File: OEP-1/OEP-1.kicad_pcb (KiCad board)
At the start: 2 copper layers, 18 parts

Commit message: готова трассировка, подготовлены файлы производства (45х30)мм)
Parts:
- added C1: Конденсатор_К10-83-25В-0,1_мкФ+-20проц., MOTOR_RLC:Конденсатор_SMD_IEC_0805, F.Cu at (109.2, 155.8)
- added C2: Конденсатор_К53-56А-32В-22_мкФ+-10проц., MOTOR_RLC:Конденсатор_тантал_SMD_m7343, F.Cu at (133.5, 148.2)
- added C3: Конденсатор_К10-83-25В-0,1_мкФ+-20проц., MOTOR_RLC:Конденсатор_SMD_IEC_0805, F.Cu at (117.0, 157.2)
- added C4: Конденсатор_К10-83-25В-0,1_мкФ+-20проц., MOTOR_RLC:Конденсатор_SMD_IEC_0805, F.Cu at (127.2, 159.0)
- added C5: Конденсатор_К10-83-25В-0,1_мкФ+-20проц., MOTOR_RLC:Конденсатор_SMD_IEC_0805, F.Cu at (125.0, 159.0)
- added C6: Конденсатор_К10-83-25В-0,1_мкФ+-20проц., MOTOR_RLC:Конденсатор_SMD_IEC_0805, F.Cu at (137.2, 147.5)
- added R13: Резистор_0,125Вт, MOTOR_RLC:Резистор_SMD_IEC_0805_0,125_Вт, F.Cu at (112.0, 167.2)
- added R14: Резистор_0,125Вт, MOTOR_RLC:Резистор_SMD_IEC_0805_0,125_Вт, F.Cu at (133.0, 152.5)
- added X1: Клеммник_х6, MOTOR_X:Вилка_СНП389-6ВП32-1-1, F.Cu at (105.5, 153.4)
- added X2: Клеммник_х6, MOTOR_X:Вилка_СНП389-6ВП32-1-1, F.Cu at (139.5, 166.2)
- added X3: Контрольная_точка_сопряжения, MOTOR_X:Пробник, B.Cu at (109.8, 156.0)
- added X4: Крепежное_отверстие_М3, MOTOR_ICO:Крепежное_Отверстие_под_М3, F.Cu at (103.0, 172.0)
- added X5: Крепежное_отверстие_М3, MOTOR_ICO:Крепежное_Отверстие_под_М3, F.Cu at (102.8, 147.8)
- added X6: Крепежное_отверстие_М3, MOTOR_ICO:Крепежное_Отверстие_под_М3, F.Cu at (142.0, 172.0)
- added X7: Крепежное_отверстие_М3, MOTOR_ICO:Крепежное_Отверстие_под_М3, F.Cu at (142.0, 148.0)
- R1, R10, R11, R12, R2, R3, R4, R5, R6, R7, R8, R9: footprint N_RLC:Резистор_SMD_0805_0,125Вт -> MOTOR_RLC:Резистор_SMD_IEC_0805_0,125_Вт
- moved R9 194.7 mm to (131.0, 170.8), turned to 180 degrees
- moved R4 193.4 mm to (123.0, 167.8), turned to 270 degrees
- moved DD1 187.8 mm to (111.2, 159.8), turned to 90 degrees
- moved R11 186.9 mm to (126.5, 163.0)
- moved VT1 186.8 mm to (119.2, 167.5), turned to 180 degrees
- moved VT2 183.6 mm to (130.0, 167.5), turned to 180 degrees
- moved R5 182.3 mm to (120.2, 170.8), turned to 180 degrees
- moved R1 180.8 mm to (112.2, 164.0), turned to 180 degrees
- moved R8 178.9 mm to (133.8, 167.8), turned to 270 degrees
- moved R6 176.2 mm to (126.8, 153.8), turned to 180 degrees
- moved R3 175.0 mm to (125.5, 167.8), turned to 270 degrees
- moved R10 174.7 mm to (136.2, 167.8), turned to 270 degrees
- moved DD2 174.6 mm to (133.8, 159.9), turned to 270 degrees
- moved R2 173.3 mm to (115.0, 154.0)
- moved R12 173.0 mm to (132.8, 155.8)
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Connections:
- DD1 pad 6: Net-(DD1-Pad6) -> /CAN-L-1
- DD1 pad 7: Net-(DD1-Pad7) -> /CAN-H-1
- DD2 pad 6: Net-(DD2-Pad6) -> /CAN-L-2
- DD2 pad 7: Net-(DD2-Pad7) -> /CAN-H-2
- G1 pad 1: Net-(G1-Pad1) -> /PWR
- G1 pad 3: Net-(G1-Pad3) -> /5V
- G1 pad 4: Net-(G1-Pad4) -> /GND
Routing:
- net /5V: track 0.00 -> 126.1 mm, vias 0 -> 2
- net /PWR: track 0.00 -> 68.9 mm
- net /TX-1: track 0.00 -> 63.3 mm, vias 0 -> 2
- net /PWR_GND: track 0.00 -> 60.2 mm
- net /GND: track 0.00 -> 45.0 mm, vias 0 -> 9
- net /TX-2: track 0.00 -> 35.2 mm
- net /CAN-L-1: track 0.00 -> 20.0 mm
- net /CAN-L-2: track 0.00 -> 19.9 mm
- net /RX-1: track 0.00 -> 15.9 mm, vias 0 -> 2
- net /RX-2: track 0.00 -> 13.2 mm, vias 0 -> 2
- net Net-(R13-Pad1): track 0.00 -> 10.4 mm
- net Net-(R14-Pad1): track 0.00 -> 10.4 mm
- net Net-(R8-Pad2): track 0.00 -> 7.16 mm
- net Net-(R4-Pad2): track 0.00 -> 7.16 mm
- net Net-(DA1-Pad6): track 0.00 -> 6.96 mm
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- added copper zone on B.Cu, net /GND
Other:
- board outline added: 45 x 30 mm
- net class 5V added: clearance 0.2, trace_width 0.45, via_dia 0.8, via_drill 0.4
- net class PWR added: clearance 0.4, trace_width 1, via_dia 0.8, via_drill 0.4
- board text added: "OEP-1-0N6"

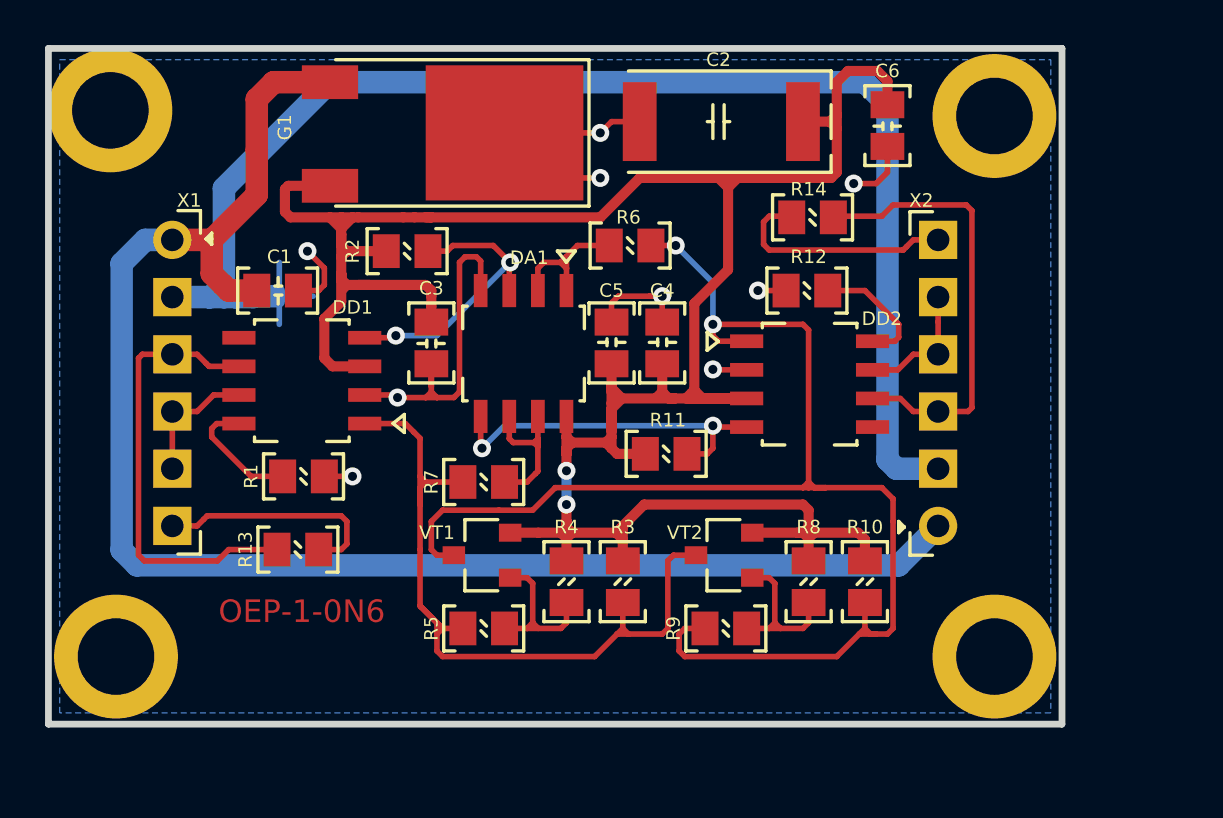
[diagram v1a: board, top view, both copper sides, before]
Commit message: ОУ заменен на транзисторный каскад (50х30 мм)
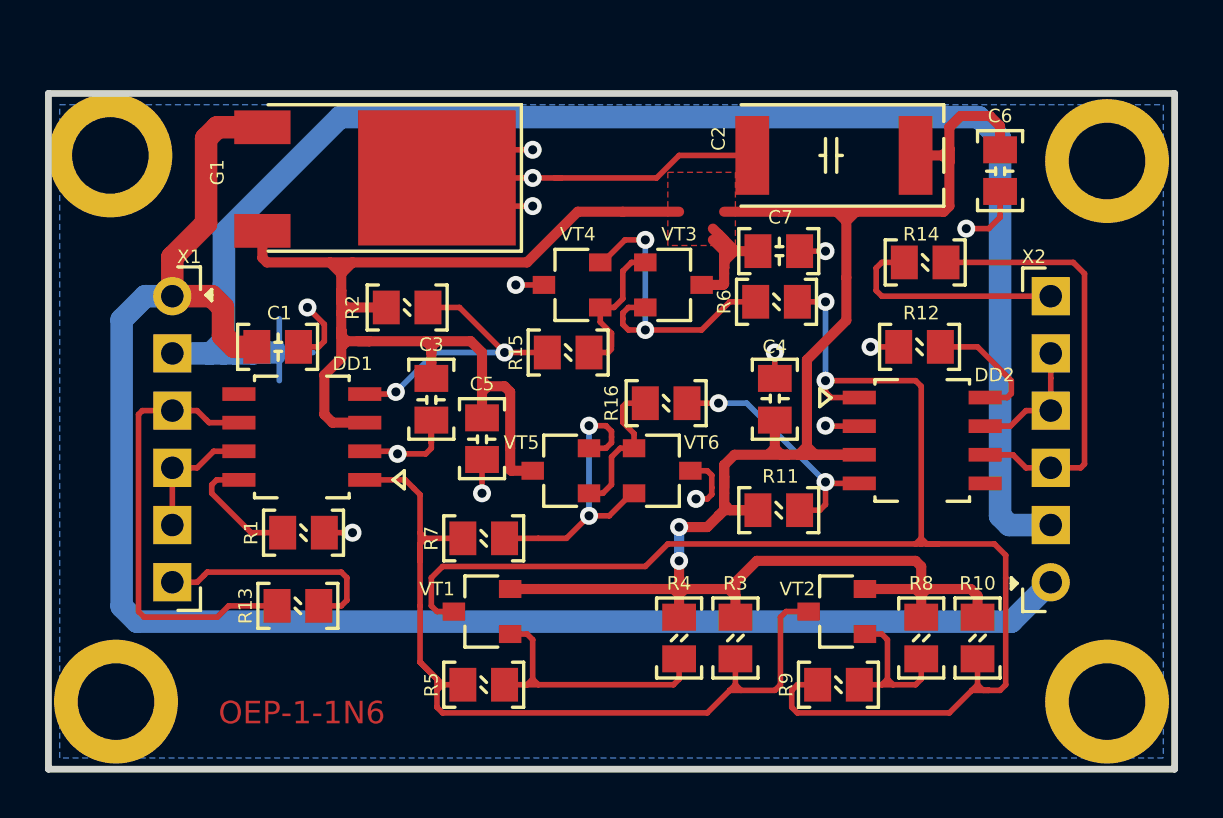
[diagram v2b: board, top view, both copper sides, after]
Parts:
- removed DA1: ОУ_LMx58, N_DD:SO-8
- added C7: Конденсатор_К10-83-25В-0,1_мкФ+-20проц., N_RLC:Конденсатор_SMD_IEC_0805, F.Cu at (131.5, 154.0)
- added R15: Резистор_0,125Вт, N_RLC:Резистор_SMD_IEC_0805_0,125_Вт, F.Cu at (124.0, 158.5)
- added R16: Резистор_0,125Вт, N_RLC:Резистор_SMD_IEC_0805_0,125_Вт, F.Cu at (126.5, 160.8)
- added VT3: Транзистор_2Т3130А9, N_VD_HL:Корпус_КТ-46, F.Cu at (127.8, 155.5)
- added VT4: Транзистор_2Т3129Г9, N_VD_HL:Корпус_КТ-46, F.Cu at (123.2, 155.5)
- added VT5: Транзистор_2Т3130А9, N_VD_HL:Корпус_КТ-46, F.Cu at (122.8, 163.8)
- added VT6: Транзистор_2Т3129Г9, N_VD_HL:Корпус_КТ-46, F.Cu at (127.2, 163.8)
- C5: footprint MOTOR_RLC:Конденсатор_SMD_IEC_0805 -> N_RLC:Конденсатор_SMD_IEC_0805
- moved R6 6.96 mm to (133.2, 156.2)
- moved C5 6.23 mm to (119.3, 161.4), turned to 270 degrees
- moved C4 5.59 mm to (132.2, 161.5)
- moved DD2 5.59 mm to (138.8, 162.4)
- moved R10 5.59 mm to (141.2, 170.2)
- moved R11 5.59 mm to (131.5, 165.5)
- moved R12 5.59 mm to (137.8, 158.2)
- moved R3 5.59 mm to (130.5, 170.2)
- moved R4 5.59 mm to (128.0, 170.2)
- moved R8 5.59 mm to (138.8, 170.3)
- moved R9 5.59 mm to (136.0, 173.2)
- moved VT2 5.59 mm to (135.0, 170.0)
- moved X2 5.59 mm to (144.5, 168.8)
- moved C6 5.39 mm to (142.2, 149.5)
- moved R14 5.39 mm to (138.0, 154.5)
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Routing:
- net /5V: track 126.1 -> 151.8 mm
- net Net-(R6-Pad2): track 6.31 -> 14.5 mm, vias 0 -> 2
- net /GND: track 45.0 -> 52.9 mm, vias 9 -> 14
- net Net-(R16-Pad1): track 0.00 -> 6.67 mm
- net /PWR_GND: track 60.2 -> 66.9 mm
- net Net-(R15-Pad1): track 0.00 -> 6.57 mm
- net Net-(R7-Pad1): track 6.96 -> 13.3 mm, vias 0 -> 2
- net /TX-2: track 35.2 -> 40.2 mm
- net Net-(R4-Pad2): track 7.16 -> 12.2 mm
- net /RX-1: track 15.9 -> 11.4 mm
- net /TX-1: track 63.3 -> 67.6 mm
- net /PWR: track 68.9 -> 73.2 mm
- added copper zone on F.Cu, net /5V
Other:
- board size 45 x 30 mm -> 50 x 30 mm
- board text added: "OEP-1-1N6"
- board text removed: "OEP-1-0N6"

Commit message: причесана трассировка, добавлены gerber-файлы
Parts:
- added R17: Резистор_0,125Вт, N_RLC:Резистор_SMD_IEC_0805_0,125_Вт, F.Cu at (129.6, 158.8)
- added R18: Резистор_0,125Вт, N_RLC:Резистор_SMD_IEC_0805_0,125_Вт, F.Cu at (124.5, 160.8)
- moved R16 1.41 mm to (127.5, 161.8)
- moved VT5 1.00 mm to (122.8, 164.8)
- moved VT6 1.00 mm to (127.2, 164.8)
- moved R7 0.25 mm to (120.0, 166.8)
- moved X1 0.25 mm to (105.5, 155.7)
- moved X3 0.25 mm to (109.8, 158.2)
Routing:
- net Net-(R18-Pad2): track 13.3 -> 18.7 mm
- net /PWR: track 73.2 -> 77.2 mm
- net Net-(R17-Pad1): track 14.5 -> 18.4 mm
- net Net-(R15-Pad1): track 6.57 -> 9.95 mm
- net Net-(R16-Pad1): track 6.67 -> 9.86 mm
- net /TX-1: track 67.6 -> 65.5 mm, vias 2 -> 3
- net /5V: track 151.8 -> 153.8 mm, vias 2 -> 4
- net /GND: track 52.9 -> 54.6 mm
- net /RX-1: track 11.4 -> 9.96 mm
- net Net-(R4-Pad2): track 12.2 -> 13.2 mm
- net /CAN-L-1: track 20.0 -> 20.9 mm
- net Net-(R13-Pad1): track 10.4 -> 11.2 mm
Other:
- net class PWR: trace_width 1 -> 0.8
- board text added: "1,5A MAX"
